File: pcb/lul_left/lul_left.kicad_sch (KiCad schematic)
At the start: 42 parts, among them J1 JST Connector, J2 JST Connector, SW1 SW_Push, SW10 SW_Push, SW11 SW_Push, SW12 SW_Push, SW13 SW_Push, SW14 SW_Push, SW15 SW_Push, SW16 SW_Push, SW17 SW_Push, SW18 SW_Push, SW19 SW_Push, SW2 SW_Push, SW20 SW_Push, SW21 SW_Push, SW22 SW_Push, SW23 SW_Push, SW24 SW_Push, SW25 SW_Push, SW26 SW_Push, SW27 SW_Push, SW28 SW_Push, SW29 SW_Push, SW3 SW_Push, SW30 SW_Push, SW31 SW_Push, SW32 SW_Push, SW33 SW_Push, SW34 SW_Push, SW4 SW_Push, SW5 SW_Push, SW6 SW_Push, SW7 SW_Push, SW8 SW_Push, SW9 SW_Push, U1 nice_nano, U2 nice_nano

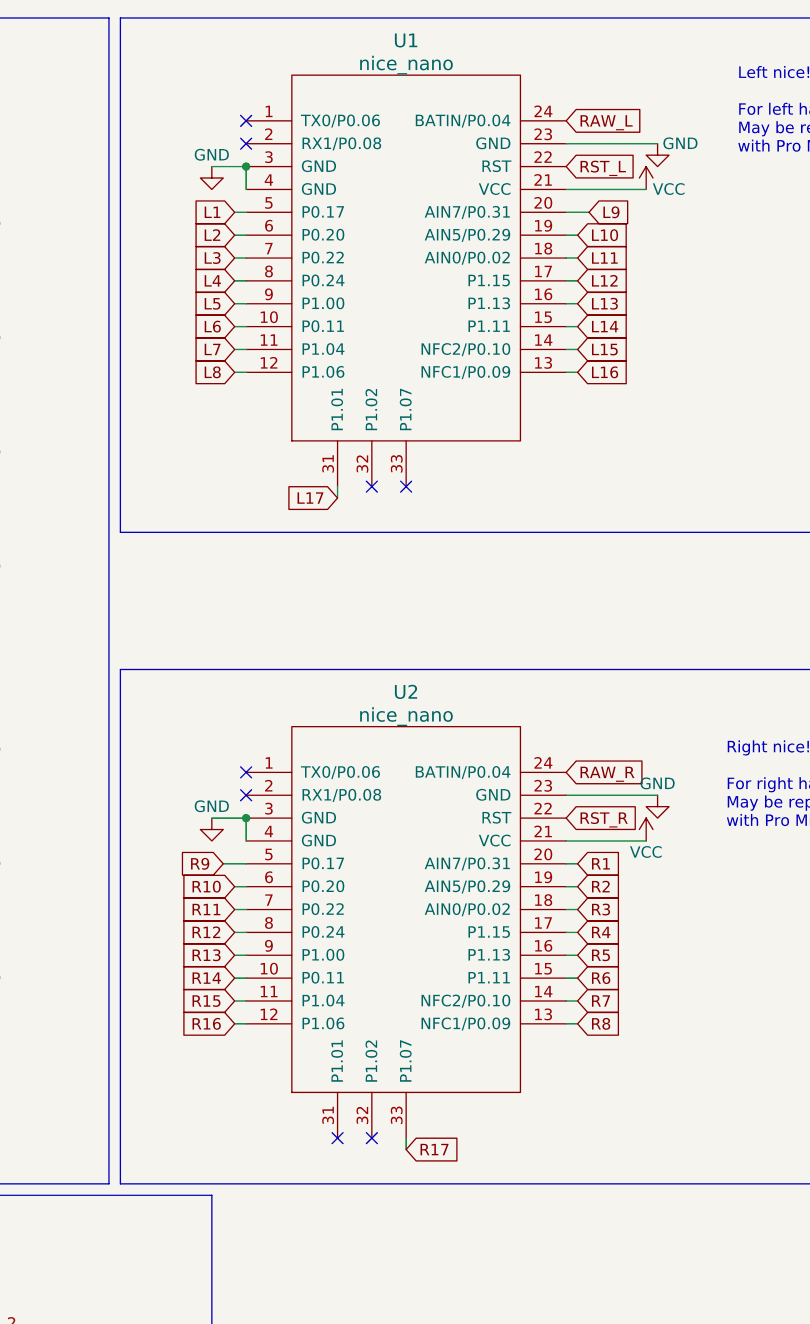
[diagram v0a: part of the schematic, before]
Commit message: move components, add dimension labels, add breakable tabs between pcb bodies
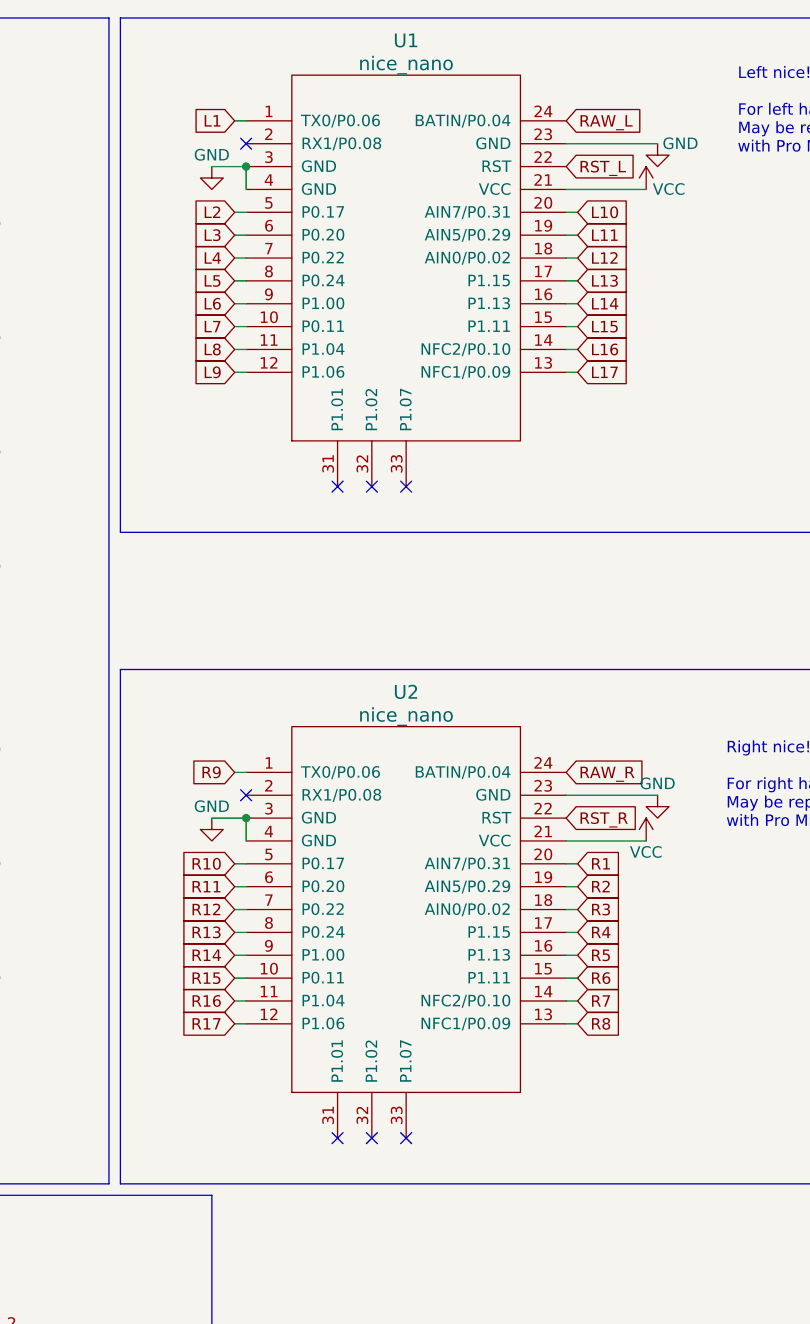
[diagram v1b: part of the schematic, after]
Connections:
- net L1: now also U1.1 (TX0/P0.06); no longer U1.5 (P0.17)
- net L10: now also U1.20 (AIN7/P0.31); no longer U1.19 (AIN5/P0.29)
- net L11: now also U1.19 (AIN5/P0.29); no longer U1.18 (AIN0/P0.02)
- net L12: now also U1.18 (AIN0/P0.02); no longer U1.17 (P1.15)
- net L13: now also U1.17 (P1.15); no longer U1.16 (P1.13)
- net L14: now also U1.16 (P1.13); no longer U1.15 (P1.11)
- net L15: now also U1.15 (P1.11); no longer U1.14 (NFC2/P0.10)
- net L16: now also U1.14 (NFC2/P0.10); no longer U1.13 (NFC1/P0.09)
- net L17: now also U1.13 (NFC1/P0.09); no longer U1.31 (P1.01)
- net L2: now also U1.5 (P0.17); no longer U1.6 (P0.20)
- net L3: now also U1.6 (P0.20); no longer U1.7 (P0.22)
- net L4: now also U1.7 (P0.22); no longer U1.8 (P0.24)
- net L5: now also U1.8 (P0.24); no longer U1.9 (P1.00)
- net L6: now also U1.9 (P1.00); no longer U1.10 (P0.11)
- net L7: now also U1.10 (P0.11); no longer U1.11 (P1.04)
- net L8: now also U1.11 (P1.04); no longer U1.12 (P1.06)
- net L9: now also U1.12 (P1.06); no longer U1.20 (AIN7/P0.31)
- net R10: now also U2.5 (P0.17); no longer U2.6 (P0.20)
- net R11: now also U2.6 (P0.20); no longer U2.7 (P0.22)
- net R12: now also U2.7 (P0.22); no longer U2.8 (P0.24)
- net R13: now also U2.8 (P0.24); no longer U2.9 (P1.00)
- net R14: now also U2.9 (P1.00); no longer U2.10 (P0.11)
- net R15: now also U2.10 (P0.11); no longer U2.11 (P1.04)
- net R16: now also U2.11 (P1.04); no longer U2.12 (P1.06)
- net R17: now also U2.12 (P1.06); no longer U2.33 (P1.07)
- net R9: now also U2.1 (TX0/P0.06); no longer U2.5 (P0.17)

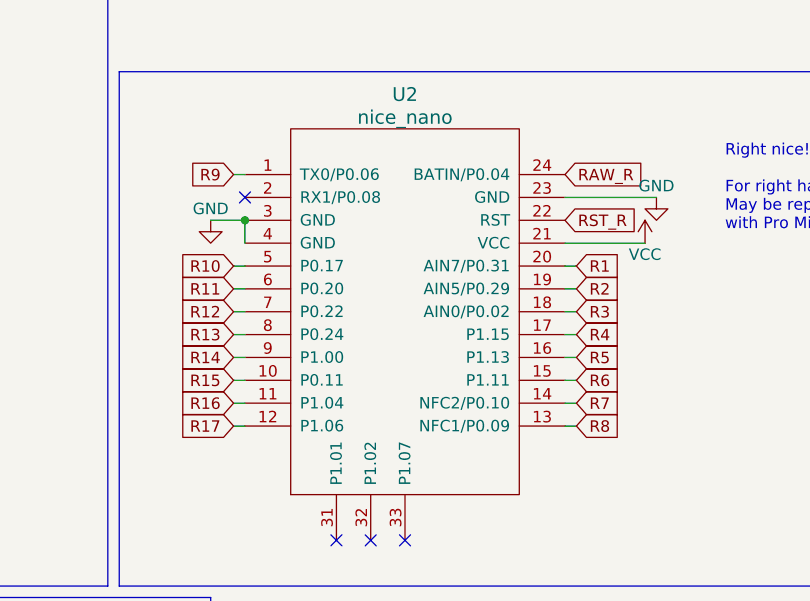
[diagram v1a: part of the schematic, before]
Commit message: route switches nicely
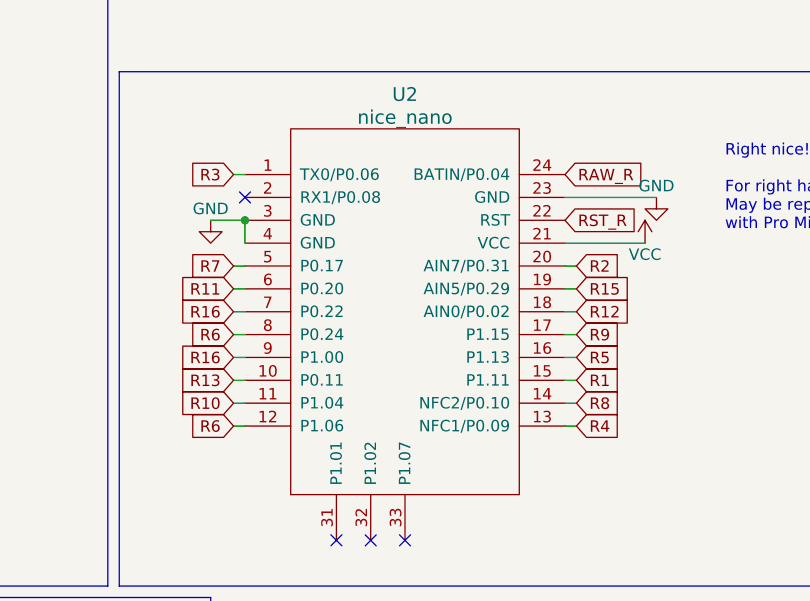
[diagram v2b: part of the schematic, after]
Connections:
- net R1: now also U2.15 (P1.11); no longer U2.20 (AIN7/P0.31)
- net R10: now also U2.11 (P1.04); no longer U2.5 (P0.17)
- net R12: now also U2.18 (AIN0/P0.02); no longer U2.7 (P0.22)
- net R13: now also U2.10 (P0.11); no longer U2.8 (P0.24)
- net R14: no longer U2.9 (P1.00)
- net R15: now also U2.19 (AIN5/P0.29); no longer U2.10 (P0.11)
- net R16: now also U2.7 (P0.22), U2.9 (P1.00); no longer U2.11 (P1.04)
- net R17: no longer U2.12 (P1.06)
- net R2: now also U2.20 (AIN7/P0.31); no longer U2.19 (AIN5/P0.29)
- net R3: now also U2.1 (TX0/P0.06); no longer U2.18 (AIN0/P0.02)
- net R4: now also U2.13 (NFC1/P0.09); no longer U2.17 (P1.15)
- net R6: now also U2.12 (P1.06), U2.8 (P0.24); no longer U2.15 (P1.11)
- net R7: now also U2.5 (P0.17); no longer U2.14 (NFC2/P0.10)
- net R8: now also U2.14 (NFC2/P0.10); no longer U2.13 (NFC1/P0.09)
- net R9: now also U2.17 (P1.15); no longer U2.1 (TX0/P0.06)
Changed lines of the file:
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@@
     (effects (font (size 1.27 1.27)) (justify left bottom))
   )
-  (global_label "R2" (shape input) (at 180.34 109.22 0) (fields_autoplaced)
-    (effects (font (size 1.27 1.27)) (justify left))
-    (property "Intersheetrefs" "${INTERSHEET_REFS}" (at 185.7253 109.22 0)
+  (global_label "R15" (shape input) (at 180.34 109.22 0) (fields_autoplaced)
+    (effects (font (size 1.27 1.27)) (justify left))
+    (property "Intersheetrefs" "${INTERSHEET_REFS}" (at 186.9348 109.22 0)
       (effects (font (size 1.27 1.27)) (justify left) hide)
     )
@@
     )
   )
-  (global_label "R6" (shape input) (at 180.34 119.38 0) (fields_autoplaced)
+  (global_label "R1" (shape input) (at 180.34 119.38 0) (fields_autoplaced)
     (effects (font (size 1.27 1.27)) (justify left))
     (property "Intersheetrefs" "${INTERSHEET_REFS}" (at 185.7253 119.38 0)
@@
     )
   )
-  (global_label "R1" (shape input) (at 180.34 106.68 0) (fields_autoplaced)
+  (global_label "R2" (shape input) (at 180.34 106.68 0) (fields_autoplaced)
     (effects (font (size 1.27 1.27)) (justify left))
     (property "Intersheetrefs" "${INTERSHEET_REFS}" (at 185.7253 106.68 0)
@@
     )
   )
-  (global_label "R12" (shape input) (at 142.24 111.76 180) (fields_autoplaced)
+  (global_label "R16" (shape input) (at 142.24 111.76 180) (fields_autoplaced)
     (effects (font (size 1.27 1.27)) (justify right))
     (property "Intersheetrefs" "${INTERSHEET_REFS}" (at 135.6452 111.76 0)
@@
     )
   )
-  (global_label "R3" (shape input) (at 180.34 111.76 0) (fields_autoplaced)
-    (effects (font (size 1.27 1.27)) (justify left))
-    (property "Intersheetrefs" "${INTERSHEET_REFS}" (at 185.7253 111.76 0)
+  (global_label "R12" (shape input) (at 180.34 111.76 0) (fields_autoplaced)
+    (effects (font (size 1.27 1.27)) (justify left))
+    (property "Intersheetrefs" "${INTERSHEET_REFS}" (at 186.9348 111.76 0)
       (effects (font (size 1.27 1.27)) (justify left) hide)
     )
@@
     )
   )
-  (global_label "R17" (shape input) (at 142.24 124.46 180) (fields_autoplaced)
-    (effects (font (size 1.27 1.27)) (justify right))
-    (property "Intersheetrefs" "${INTERSHEET_REFS}" (at 135.6452 124.46 0)
-      (effects (font (size 1.27 1.27)) (justify right) hide)
-    )
-  )
-  (global_label "R13" (shape input) (at 142.24 114.3 180) (fields_autoplaced)
-    (effects (font (size 1.27 1.27)) (justify right))
-    (property "Intersheetrefs" "${INTERSHEET_REFS}" (at 135.6452 114.3 0)
+  (global_label "R6" (shape input) (at 142.24 124.46 180) (fields_autoplaced)
+    (effects (font (size 1.27 1.27)) (justify right))
+    (property "Intersheetrefs" "${INTERSHEET_REFS}" (at 136.8547 124.46 0)
+      (effects (font (size 1.27 1.27)) (justify right) hide)
+    )
+  )
+  (global_label "R6" (shape input) (at 142.24 114.3 180) (fields_autoplaced)
+    (effects (font (size 1.27 1.27)) (justify right))
+    (property "Intersheetrefs" "${INTERSHEET_REFS}" (at 136.8547 114.3 0)
       (effects (font (size 1.27 1.27)) (justify right) hide)
     )
@@
     )
   )
-  (global_label "R7" (shape input) (at 180.34 121.92 0) (fields_autoplaced)
+  (global_label "R8" (shape input) (at 180.34 121.92 0) (fields_autoplaced)
     (effects (font (size 1.27 1.27)) (justify left))
     (property "Intersheetrefs" "${INTERSHEET_REFS}" (at 185.7253 121.92 0)
@@
     )
   )
-  (global_label "R4" (shape input) (at 180.34 114.3 0) (fields_autoplaced)
+  (global_label "R9" (shape input) (at 180.34 114.3 0) (fields_autoplaced)
     (effects (font (size 1.27 1.27)) (justify left))
     (property "Intersheetrefs" "${INTERSHEET_REFS}" (at 185.7253 114.3 0)
@@
     )
   )
-  (global_label "R14" (shape input) (at 142.24 116.84 180) (fields_autoplaced)
+  (global_label "R16" (shape input) (at 142.24 116.84 180) (fields_autoplaced)
     (effects (font (size 1.27 1.27)) (justify right))
     (property "Intersheetrefs" "${INTERSHEET_REFS}" (at 135.6452 116.84 0)
@@
     )
   )
-  (global_label "R15" (shape input) (at 142.24 119.38 180) (fields_autoplaced)
+  (global_label "R13" (shape input) (at 142.24 119.38 180) (fields_autoplaced)
     (effects (font (size 1.27 1.27)) (justify right))
     (property "Intersheetrefs" "${INTERSHEET_REFS}" (at 135.6452 119.38 0)
@@
     )
   )
-  (global_label "R8" (shape input) (at 180.34 124.46 0) (fields_autoplaced)
+  (global_label "R4" (shape input) (at 180.34 124.46 0) (fields_autoplaced)
     (effects (font (size 1.27 1.27)) (justify left))
     (property "Intersheetrefs" "${INTERSHEET_REFS}" (at 185.7253 124.46 0)
@@
     )
   )
-  (global_label "R9" (shape input) (at 142.24 96.52 180) (fields_autoplaced)
+  (global_label "R3" (shape input) (at 142.24 96.52 180) (fields_autoplaced)
     (effects (font (size 1.27 1.27)) (justify right))
     (property "Intersheetrefs" "${INTERSHEET_REFS}" (at 136.8547 96.52 0)
@@
     )
   )
-  (global_label "R10" (shape input) (at 142.24 106.68 180) (fields_autoplaced)
-    (effects (font (size 1.27 1.27)) (justify right))
-    (property "Intersheetrefs" "${INTERSHEET_REFS}" (at 135.6452 106.68 0)
-      (effects (font (size 1.27 1.27)) (justify right) hide)
-    )
-  )
-  (global_label "R16" (shape input) (at 142.24 121.92 180) (fields_autoplaced)
+  (global_label "R7" (shape input) (at 142.24 106.68 180) (fields_autoplaced)
+    (effects (font (size 1.27 1.27)) (justify right))
+    (property "Intersheetrefs" "${INTERSHEET_REFS}" (at 136.8547 106.68 0)
+      (effects (font (size 1.27 1.27)) (justify right) hide)
+    )
+  )
+  (global_label "R10" (shape input) (at 142.24 121.92 180) (fields_autoplaced)
     (effects (font (size 1.27 1.27)) (justify right))
     (property "Intersheetrefs" "${INTERSHEET_REFS}" (at 135.6452 121.92 0)
